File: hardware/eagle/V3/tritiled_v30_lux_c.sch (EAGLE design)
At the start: 12 parts, among them IC1 PIC12LF1571, IC2 74LVC1G123, Q1 IRLML6244, Q2 DMG2305UX

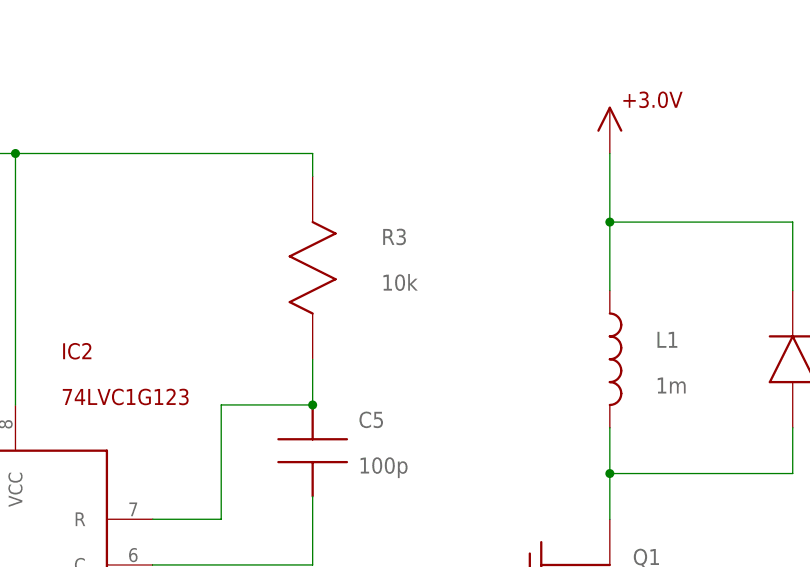
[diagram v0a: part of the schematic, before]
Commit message: correct values for R3
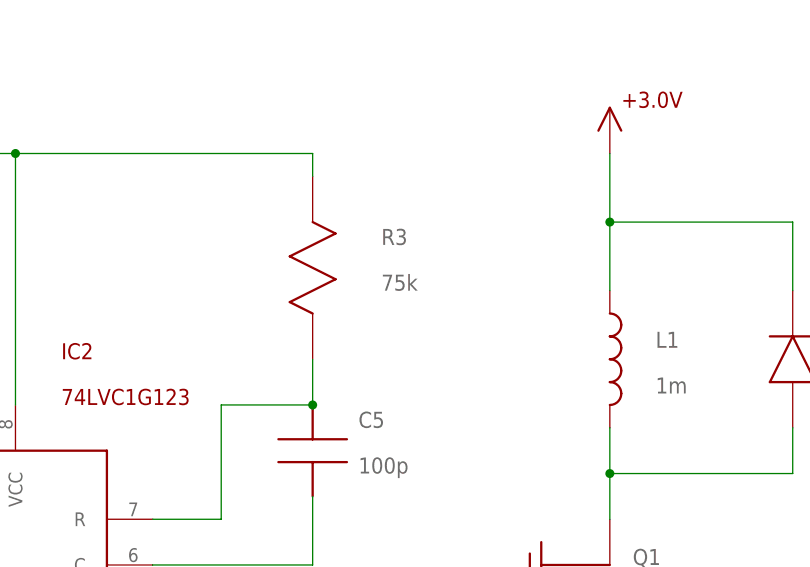
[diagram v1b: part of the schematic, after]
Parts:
- R3: value 10k -> 75k
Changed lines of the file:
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@@
 <?xml version="1.0" encoding="utf-8"?>
 <!DOCTYPE eagle SYSTEM "eagle.dtd">
-<eagle version="8.2.2">
+<eagle version="8.5.0">
 <drawing>
 <settings>
 <setting alwaysvectorfont="yes"/>
+<setting keepoldvectorfont="yes"/>
 <setting verticaltext="up"/>
 </settings>
@@
 <part name="IC2" library="tritiled" deviceset="74LVC1G123" device=""/>
 <part name="U$22" library="tritiled" deviceset="GND" device=""/>
-<part name="R3" library="tritiled" deviceset="R" device="0603" value="10k"/>
+<part name="R3" library="tritiled" deviceset="R" device="0603" value="75k"/>
 <part name="C5" library="tritiled" deviceset="C" device="0603" value="100p"/>
 <part name="Q2" library="tritiled" deviceset="DMG2305UX" device="SOT23" value="DMG2305UX"/>
